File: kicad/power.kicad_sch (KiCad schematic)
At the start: 9 parts, among them J1 USB_C_Receptacle_USB2.0_16P, U1 NCP1117-3.3_SOT223

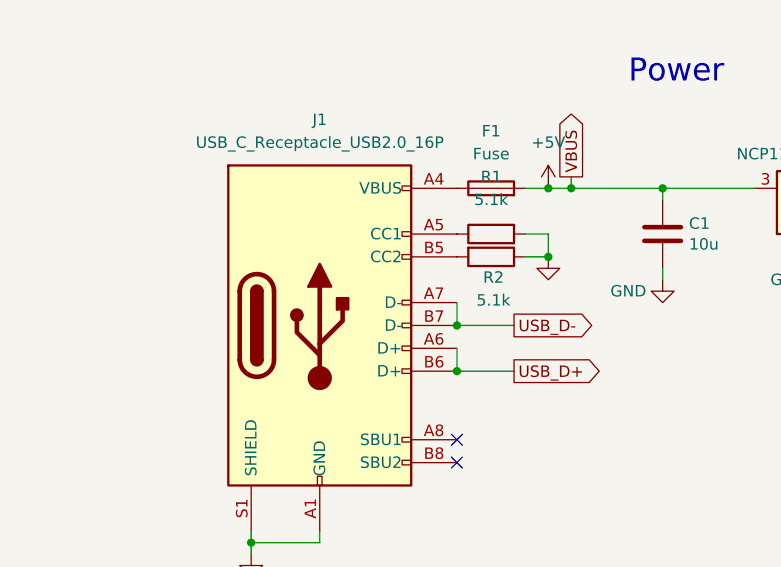
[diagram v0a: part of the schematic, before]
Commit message: actual attempt at source controlling kicad project
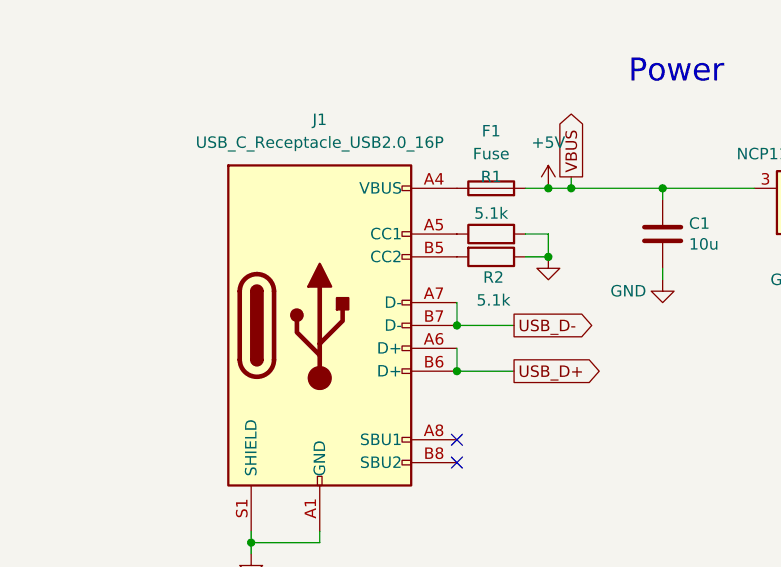
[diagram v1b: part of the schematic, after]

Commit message: moving things around
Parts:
- renumbered D67 to D1, R11 to R1, R1 to R2, R2 to R3
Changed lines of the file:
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@@
 		(dnp no)
 		(fields_autoplaced yes)
-		(property "Reference" "R11"
+		(property "Reference" "R1"
 			(at 129.54 99.0599 0)
 			(effects
@@
 			(project ""
 				(path "/6dbb65f4-5576-4e18-9627-83014d84ecc4/69cff255-9fa6-4711-8724-a2455d867f76"
-					(reference "R11")
+					(reference "R1")
 					(unit 1)
 				)
@@
 		(on_board yes)
 		(dnp no)
-		(property "Reference" "R1"
+		(property "Reference" "R2"
 			(at 81.28 95.25 90)
 			(effects
@@
 			(project ""
 				(path "/6dbb65f4-5576-4e18-9627-83014d84ecc4/69cff255-9fa6-4711-8724-a2455d867f76"
-					(reference "R1")
+					(reference "R2")
 					(unit 1)
 				)
@@
 		(dnp no)
 		(fields_autoplaced yes)
-		(property "Reference" "D67"
+		(property "Reference" "D1"
 			(at 130.81 108.2674 90)
 			(effects
@@
 			(project ""
 				(path "/6dbb65f4-5576-4e18-9627-83014d84ecc4/69cff255-9fa6-4711-8724-a2455d867f76"
-					(reference "D67")
+					(reference "D1")
 					(unit 1)
 				)
@@
 		(on_board yes)
 		(dnp no)
-		(property "Reference" "#PWR032"
+		(property "Reference" "#PWR09"
 			(at 127 118.11 0)
 			(effects
@@
 			(project "keyboard"
 				(path "/6dbb65f4-5576-4e18-9627-83014d84ecc4/69cff255-9fa6-4711-8724-a2455d867f76"
-					(reference "#PWR032")
+					(reference "#PWR09")
 					(unit 1)
 				)
@@
 		(on_board yes)
 		(dnp no)
-		(property "Reference" "R2"
+		(property "Reference" "R3"
 			(at 81.534 106.426 90)
 			(effects
@@
 			(project "keyboard"
 				(path "/6dbb65f4-5576-4e18-9627-83014d84ecc4/69cff255-9fa6-4711-8724-a2455d867f76"
-					(reference "R2")
+					(reference "R3")
 					(unit 1)
 				)
@@
 		(on_board yes)
 		(dnp no)
-		(property "Reference" "#PWR09"
+		(property "Reference" "#PWR010"
 			(at 54.61 143.51 0)
 			(effects
@@
 			(project "keyboard"
 				(path "/6dbb65f4-5576-4e18-9627-83014d84ecc4/69cff255-9fa6-4711-8724-a2455d867f76"
-					(reference "#PWR09")
-					(unit 1)
-				)
+					(reference "#PWR010")
+					(unit 1)
+				)
